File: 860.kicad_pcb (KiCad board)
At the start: 4 copper layers, 38 x 106 mm, 160 parts, among them J1 PJ301B, J2 PJ301B, J3 PJ301B, J4 PJ301B, J5 PJ301B, J6 PJ301B, P1 CONN_02X05, Q1 BCM857BS, Q2 BCM857BS, Q3 J112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

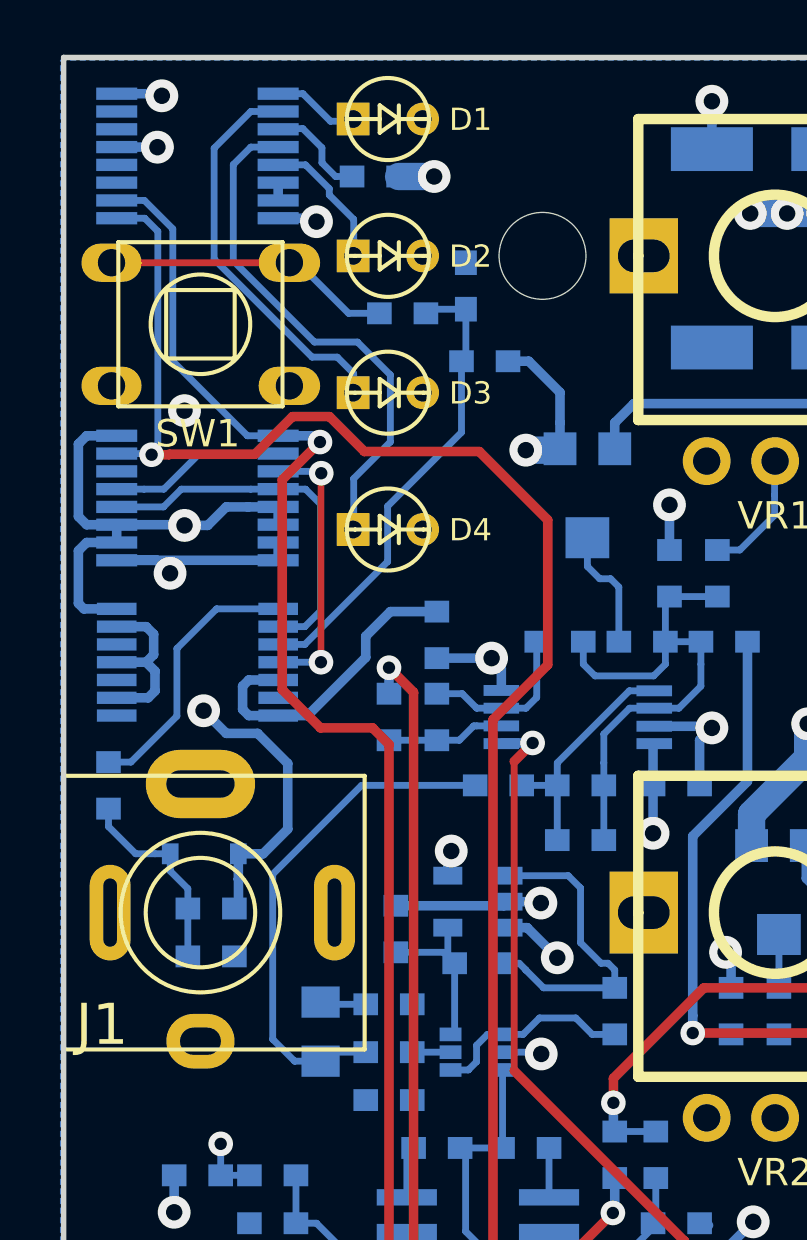
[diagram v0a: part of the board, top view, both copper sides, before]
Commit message: silk screen adjust on 860 PCB, alignment check of backplane: OK
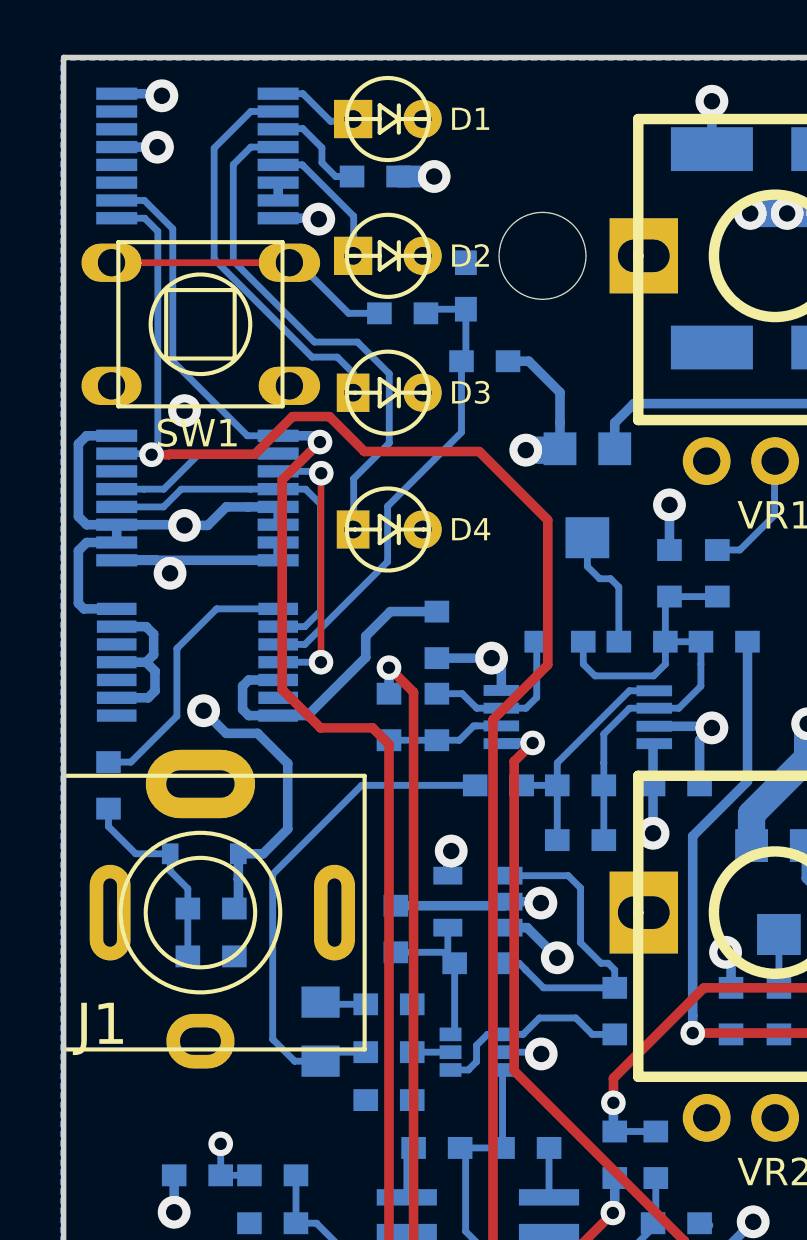
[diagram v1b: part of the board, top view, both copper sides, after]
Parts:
- added G***: LOGO, LOGO, B.Cu at (115.8, 75.0)

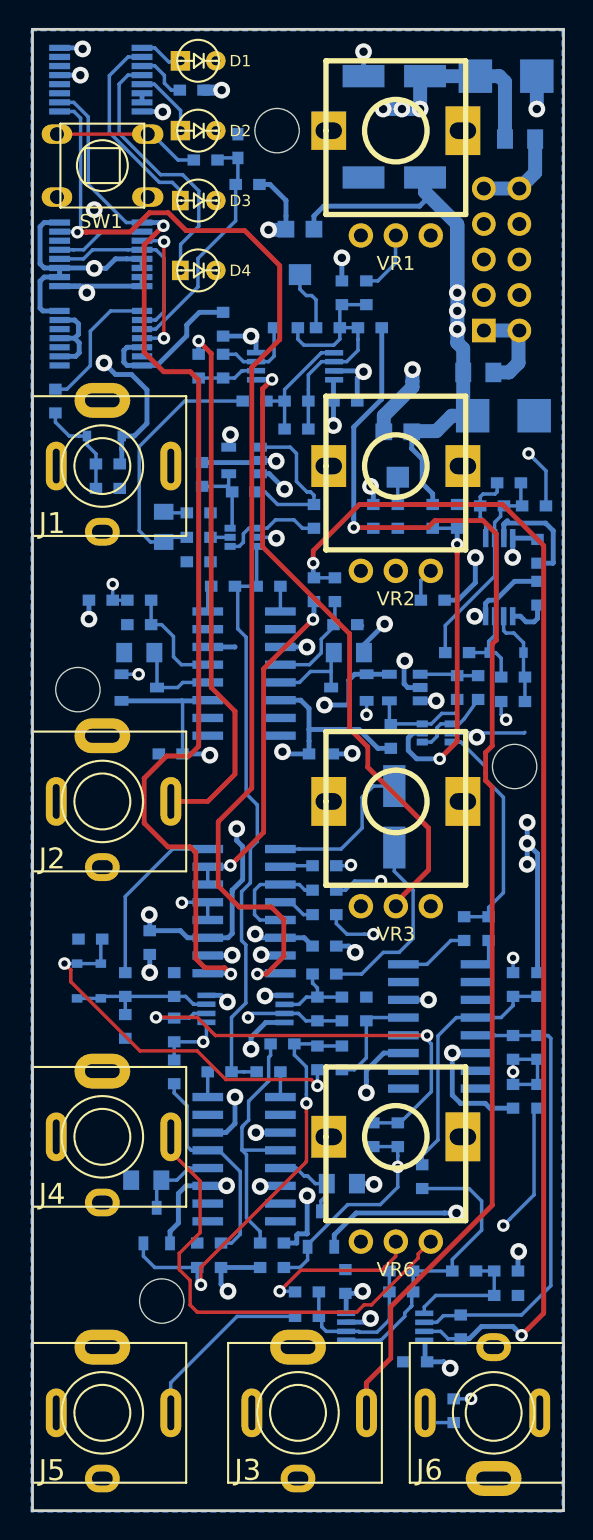
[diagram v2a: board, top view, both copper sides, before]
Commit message: ordered next revision PCB for testing, fitting, added backplane
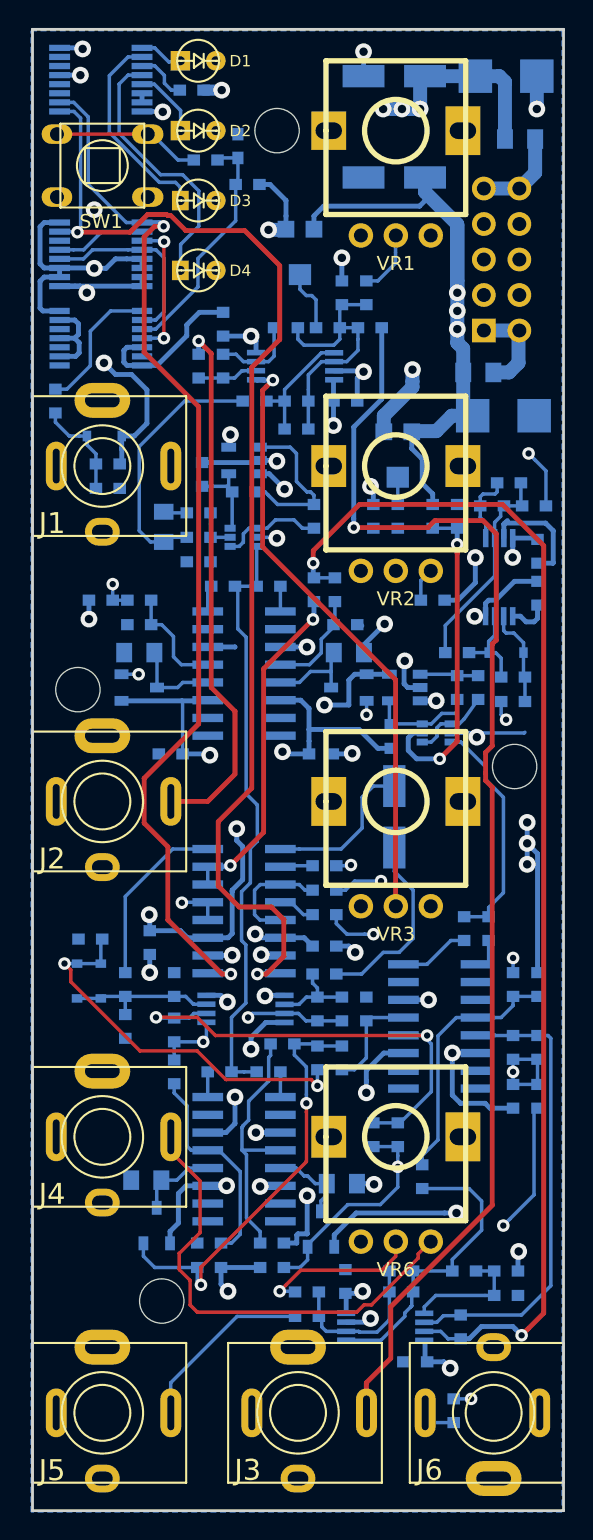
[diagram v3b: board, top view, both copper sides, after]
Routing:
- net Net-(U10-Pad1): track 79.3 -> 76.3 mm
- net Net-(U1-Pad5): track 45.0 -> 43.1 mm

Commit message: silk screen fiddling before panelization
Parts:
- removed the G*** at (114.0, 109.2)
- removed the G*** at (122.7, 121.3)
- added G***: LOGO, w_logo:Logo_silk_Lead-Free_5x5mm, B.Cu at (115.5, 119.2)
- moved REF*** 20.5 mm to (143.1, 119.2)
- moved G*** 0.14 mm to (129.8, 119.3)
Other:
- board text added: "A"
- board text added: "B"
- board text added: "ROHS r1.3 06/19"
- board text removed: "r1.2 06/19"

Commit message: panelization
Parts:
- added REF**: fiducial-1mm, MyModules:fiducial-1mm, B.Cu at (146.2, 122.5)
- added REF**: fiducial-1mm, MyModules:fiducial-1mm, B.Cu at (111.8, 30.0)
- moved C19 0.55 mm to (130.9, 85.3)
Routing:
- net Net-(R52-Pad1): track 15.5 -> 16.7 mm
- net OUT2B: track 2.67 -> 3.24 mm
- net GND: track 107.2 -> 107.6 mm, vias 28 -> 27
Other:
- board text added: "FAST"
- board text added: "HATE"
- board text added: "HOLD"
- board text added: "LOVE"
